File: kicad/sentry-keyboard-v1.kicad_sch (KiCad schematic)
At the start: 272 parts, among them J1 USB_C_Receptacle_USB2.0, J4 AVR-ISP-6, SW1 Reset, SW2 RotaryEncoder_Switch, U1 ATmega32U4-AU, U3 PRTR5V0U2X, Y1 16Mhz

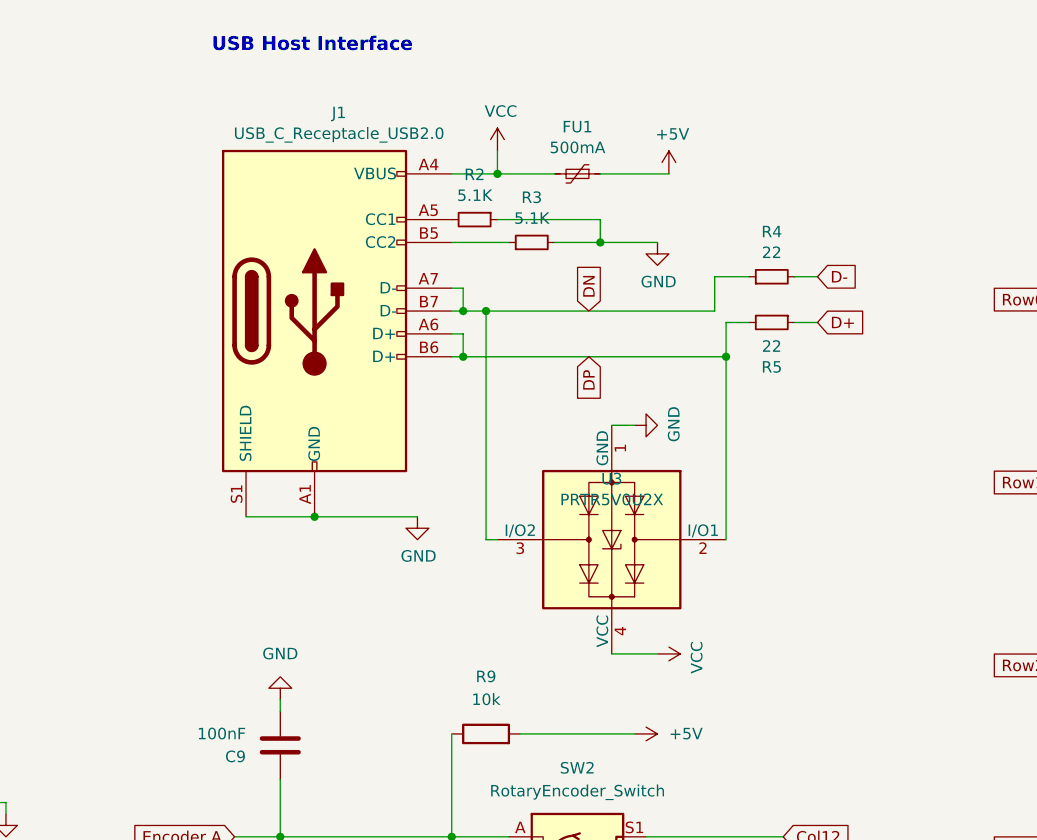
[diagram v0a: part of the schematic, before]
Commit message: Simpler USB connection
The keyboard case comes with a USBC breakout card. This card contains
the 5.1K resistors, and what looks like an ESD on them. I've removed
those from the schematics, and assigned a picoblade connector, as that
is what I think the board is currently using.
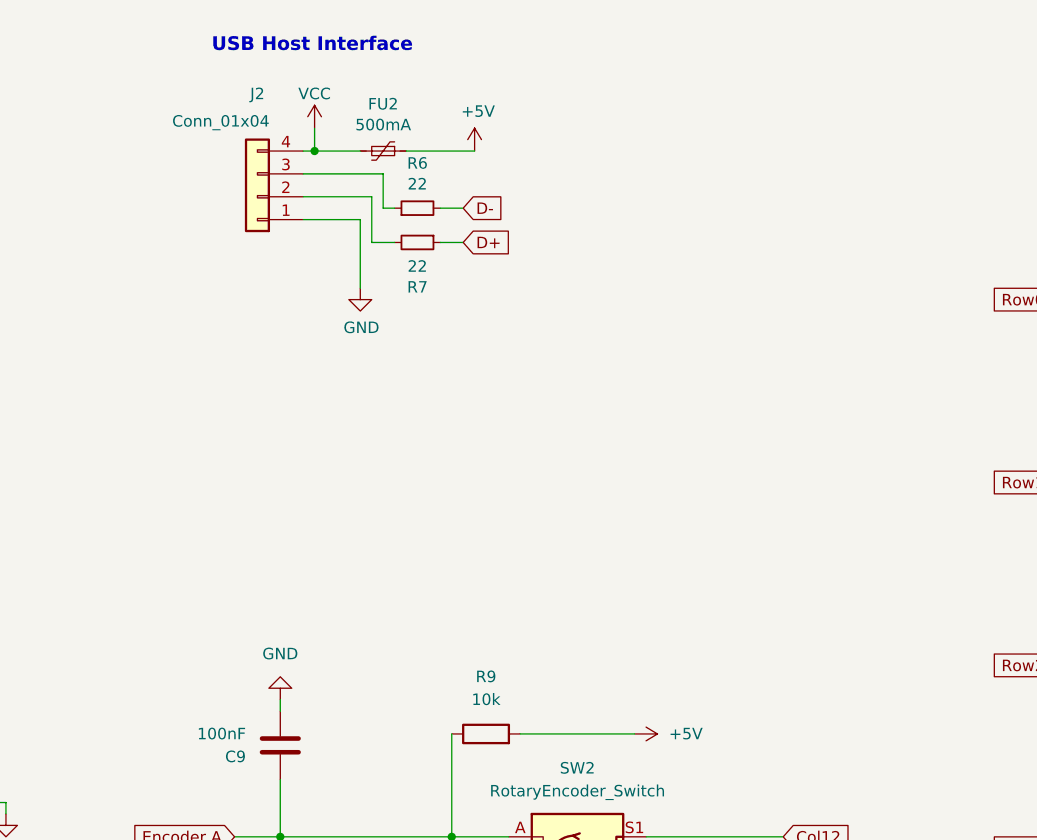
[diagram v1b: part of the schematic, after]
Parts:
- removed FU1: 500mA, Fuse:Fuse_1206_3216Metric_Pad1.42x1.75mm_HandSolder, symbol Device:Polyfuse_Small
- removed J1: USB_C_Receptacle_USB2.0, Keebio:USB_miniB_HandSolder, symbol Connector:USB_C_Receptacle_USB2.0_14P
- removed R2, R3: 5.1K, Resistor_SMD:R_0805_2012Metric, symbol Device:R_Small
- removed R4, R5: 22, Resistor_SMD:R_0805_2012Metric, symbol Device:R_Small
- removed U3: PRTR5V0U2X, Package_TO_SOT_SMD:SOT-143, symbol Power_Protection:PRTR5V0U2X
- added FU2: 500mA, Fuse:Fuse_1206_3216Metric_Pad1.42x1.75mm_HandSolder, symbol Device:Polyfuse_Small
- added J2: Conn_01x04, Connector_Molex:Molex_PicoBlade_53261-0471_1x04-1MP_P1.25mm_Horizontal, symbol Connector_Generic:Conn_01x04
- added R6, R7: 22, Resistor_SMD:R_0805_2012Metric, symbol Device:R_Small
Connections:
- net +5V: now also FU2.1
- net D+: now also R7.1
- net D-: now also R6.2
- net GND: now also J2.1 (Pin_1)
- net VCC: now also FU2.2, J2.4 (Pin_4)
- new net: J2.2 (Pin_2), R7.2
- new net: J2.3 (Pin_3), R6.1

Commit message: Update footprints and adjust positioning
I printed out the schematic and compare with the physical board and
needed to make some adjustments.
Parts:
- MXenter1: footprint Kaihl hotswap:MX-Hotswap-2.25U -> Kaihl hotswap:MX-Hotswap-2.25U-ReversedStabilizers
- MXspace1: footprint Kaihl hotswap:MX-Hotswap-6.25U -> Kaihl hotswap:MX-Hotswap-6.25U-ReversedStabilizers
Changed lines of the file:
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@@
 			)
 		)
-		(property "Footprint" "Kaihl hotswap:MX-Hotswap-6.25U"
+		(property "Footprint" "Kaihl hotswap:MX-Hotswap-6.25U-ReversedStabilizers"
 			(at 259.715 137.795 0)
 			(effects
@@
 			)
 		)
-		(property "Footprint" "Kaihl hotswap:MX-Hotswap-2.25U"
+		(property "Footprint" "Kaihl hotswap:MX-Hotswap-2.25U-ReversedStabilizers"
 			(at 352.425 97.155 0)
 			(effects

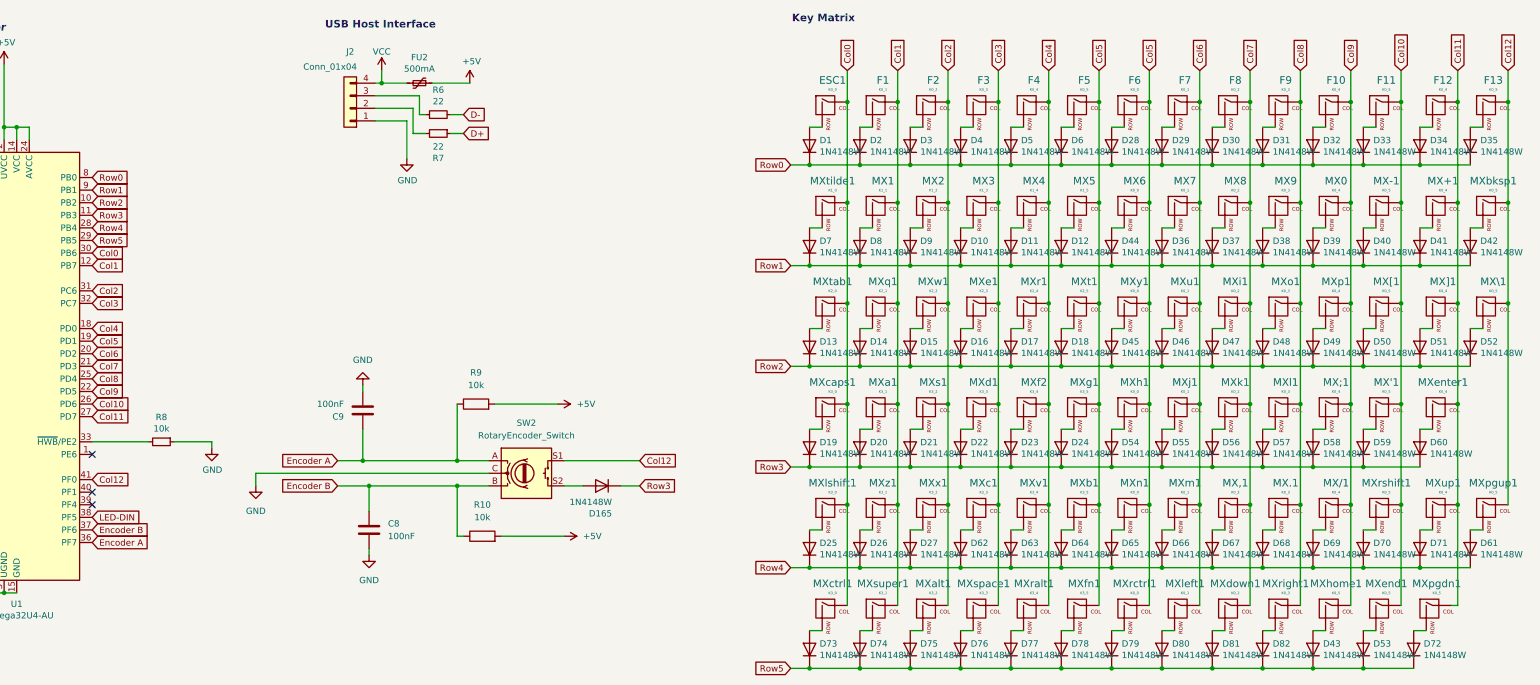
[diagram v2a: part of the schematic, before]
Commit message: Fix a big schematic mistake
I had two col5 nets! I only noticed this as I started routing the
columns. I also fixed the numbering of all the switches.
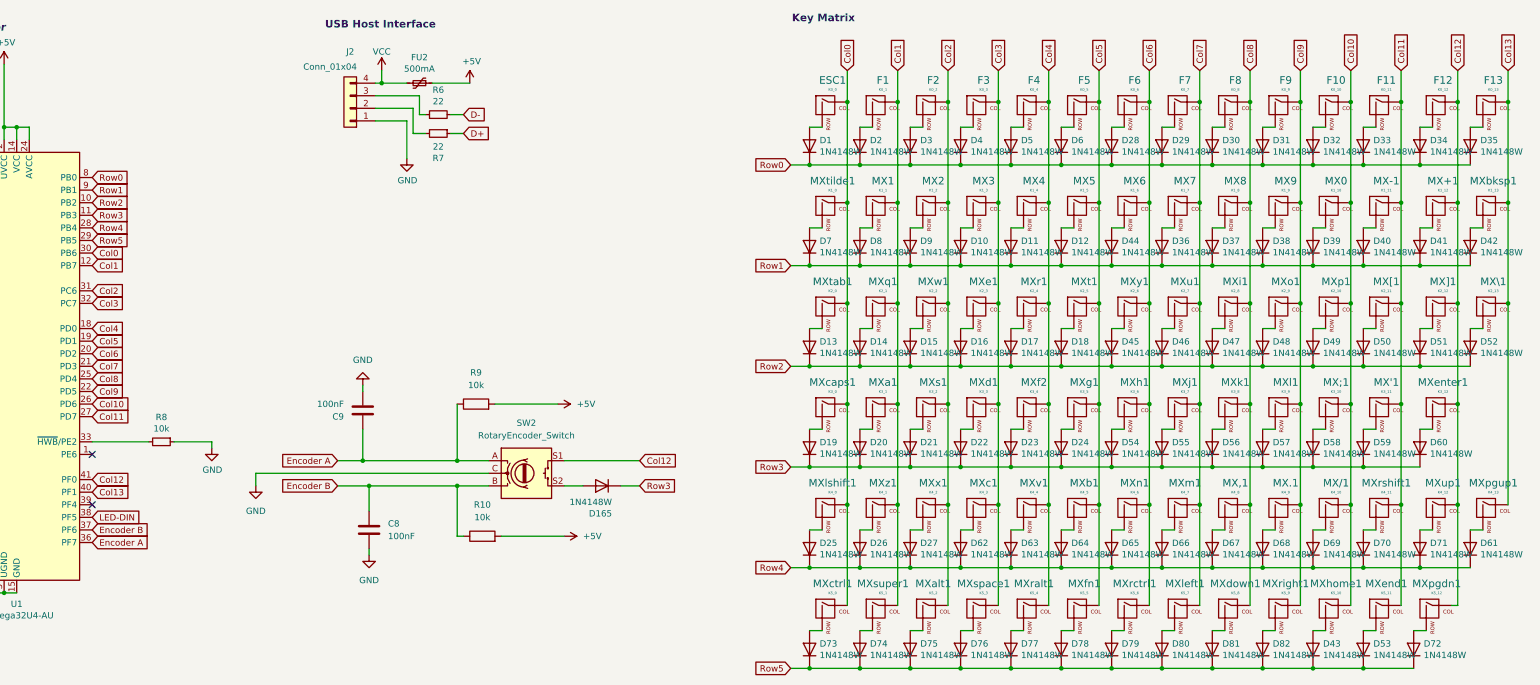
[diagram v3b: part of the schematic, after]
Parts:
- F10: value K0_4 -> K0_10
- F11: value K0_5 -> K0_11
- F12: value K0_4 -> K0_12
- F13: value K0_5 -> K0_13
- F6: value K0_0 -> K0_6
- F7: value K0_1 -> K0_7
- F8: value K0_2 -> K0_8
- F9: value K0_3 -> K0_9
- MX'1: value K0_5 -> K3_11
- MX+1: value K0_4 -> K1_12
- MX,1: value K0_2 -> K4_8
- MX-1: value K0_5 -> K1_11
- MX.1: value K0_3 -> K4_9
- MX/1: value K0_4 -> K4_10
- MX0: value K0_4 -> K1_10
- MX6: value K0_0 -> K1_6
- MX7: value K0_1 -> K1_7
- MX8: value K0_2 -> K1_8
- MX9: value K0_3 -> K1_9
- MX;1: value K0_4 -> K3_10
- MX[1: value K0_5 -> K2_11
- MX\1: value K0_5 -> K2_13
- MX]1: value K0_4 -> K2_12
- MXalt1: value K3_2 -> K5_2
- MXb1: value K3_5 -> K4_5
- MXbksp1: value K0_5 -> K1_13
- MXc1: value K3_3 -> K4_3
- MXctrl1: value K3_0 -> K5_0
- MXdown1: value K0_2 -> K5_8
- MXend1: value K0_5 -> K5_11
- MXenter1: value K0_4 -> K3_12
- MXfn1: value K3_5 -> K5_5
- MXh1: value K0_0 -> K3_6
- MXhome1: value K0_5 -> K5_10
- MXi1: value K0_2 -> K2_8
- MXj1: value K0_1 -> K3_7
- MXk1: value K0_2 -> K3_8
- MXl1: value K0_3 -> K3_9
- MXleft1: value K0_1 -> K5_7
- MXlshift1: value K3_0 -> K4_0
- MXm1: value K0_1 -> K4_7
- MXn1: value K0_0 -> K4_6
- MXo1: value K0_3 -> K2_9
- MXp1: value K0_4 -> K2_10
- MXpgdn1: value K0_5 -> K5_12
- MXpgup1: value K0_5 -> K4_13
- MXralt1: value K3_4 -> K5_4
- MXrctrl1: value K0_0 -> K5_6
- MXright1: value K0_3 -> K5_9
- MXrshift1: value K0_5 -> K4_11
- MXspace1: value K3_3 -> K5_3
- MXsuper1: value K3_1 -> K5_1
- MXu1: value K0_1 -> K2_7
- MXup1: value K0_4 -> K4_12
- MXv1: value K3_4 -> K4_4
- MXx1: value K3_2 -> K4_2
- MXy1: value K0_0 -> K2_6
- MXz1: value K3_1 -> K4_1
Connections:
- net Col10: now also F10.1 (COL), MX/1.1 (COL), MX0.1 (COL), MX;1.1 (COL), MXhome1.1 (COL), MXp1.1 (COL); no longer F11.1 (COL), MX'1.1 (COL), MX-1.1 (COL), MX[1.1 (COL), MXend1.1 (COL), MXrshift1.1 (COL)
- net Col11: now also F11.1 (COL), MX'1.1 (COL), MX-1.1 (COL), MX[1.1 (COL), MXend1.1 (COL), MXrshift1.1 (COL); no longer F12.1 (COL), MX+1.1 (COL), MX]1.1 (COL), MXenter1.1 (COL), MXpgdn1.1 (COL), MXup1.1 (COL)
- net Col12: now also F12.1 (COL), MX+1.1 (COL), MX]1.1 (COL), MXenter1.1 (COL), MXpgdn1.1 (COL), MXup1.1 (COL); no longer F13.1 (COL), MX\1.1 (COL), MXbksp1.1 (COL), MXpgup1.1 (COL)
- net Col5: no longer F6.1 (COL), MX6.1 (COL), MXh1.1 (COL), MXn1.1 (COL), MXrctrl1.1 (COL), MXy1.1 (COL)
- net Col6: now also F6.1 (COL), MX6.1 (COL), MXh1.1 (COL), MXn1.1 (COL), MXrctrl1.1 (COL), MXy1.1 (COL); no longer F7.1 (COL), MX7.1 (COL), MXj1.1 (COL), MXleft1.1 (COL), MXm1.1 (COL), MXu1.1 (COL)
- net Col7: now also F7.1 (COL), MX7.1 (COL), MXj1.1 (COL), MXleft1.1 (COL), MXm1.1 (COL), MXu1.1 (COL); no longer F8.1 (COL), MX,1.1 (COL), MX8.1 (COL), MXdown1.1 (COL), MXi1.1 (COL), MXk1.1 (COL)
- net Col8: now also F8.1 (COL), MX,1.1 (COL), MX8.1 (COL), MXdown1.1 (COL), MXi1.1 (COL), MXk1.1 (COL); no longer F9.1 (COL), MX.1.1 (COL), MX9.1 (COL), MXl1.1 (COL), MXo1.1 (COL), MXright1.1 (COL)
- net Col9: now also F9.1 (COL), MX.1.1 (COL), MX9.1 (COL), MXl1.1 (COL), MXo1.1 (COL), MXright1.1 (COL); no longer F10.1 (COL), MX/1.1 (COL), MX0.1 (COL), MX;1.1 (COL), MXhome1.1 (COL), MXp1.1 (COL)
- net Col13: now reaches U1.40 (PF1)
- net Col13: now also F13.1 (COL), MX\1.1 (COL), MXbksp1.1 (COL), MXpgup1.1 (COL)
- no-connect marks 5 -> 4

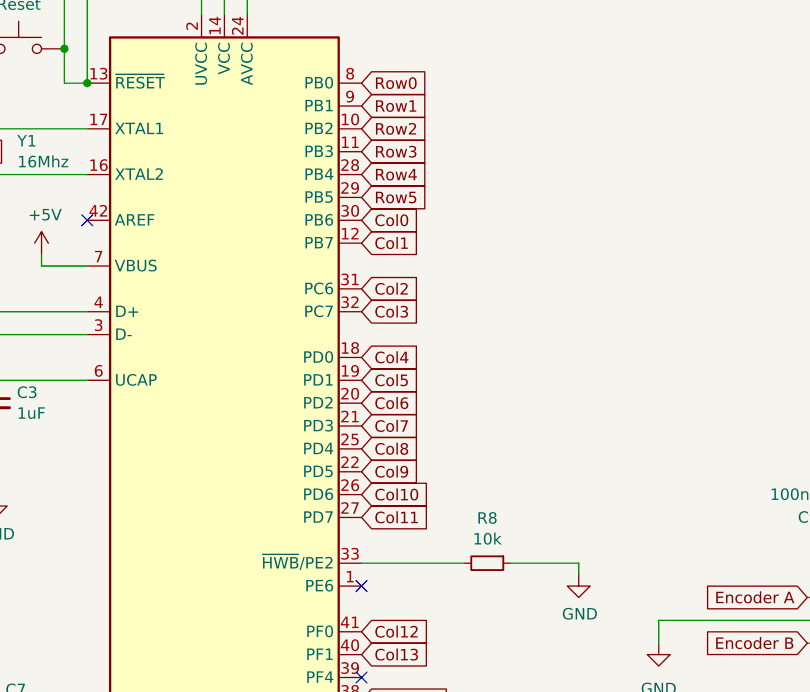
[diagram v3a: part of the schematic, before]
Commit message: Start connecting up the mcu
reassign a bunch of pins to make routing easier.
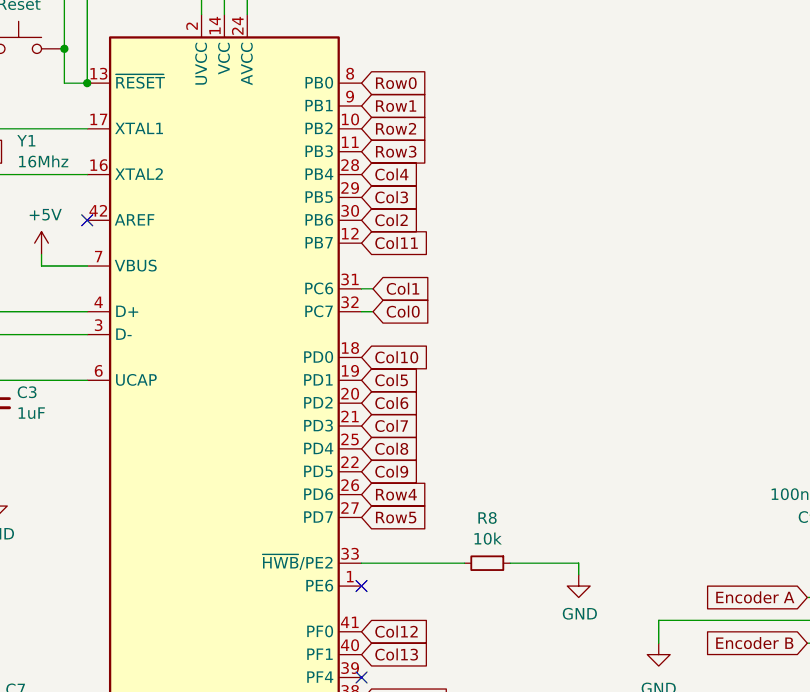
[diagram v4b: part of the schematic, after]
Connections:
- net Col0: now also U1.32 (PC7); no longer U1.30 (PB6)
- net Col1: now also U1.31 (PC6); no longer U1.12 (PB7)
- net Col10: now also U1.18 (PD0); no longer U1.26 (PD6)
- net Col11: now also U1.12 (PB7); no longer U1.27 (PD7)
- net Col2: now also U1.30 (PB6); no longer U1.31 (PC6)
- net Col3: now also U1.29 (PB5); no longer U1.32 (PC7)
- net Col4: now also U1.28 (PB4); no longer U1.18 (PD0)
- net Row4: now also U1.26 (PD6); no longer U1.28 (PB4)
- net Row5: now also U1.27 (PD7); no longer U1.29 (PB5)
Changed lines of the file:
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@@
 	(wire
 		(pts
+			(xy 96.52 72.39) (xy 97.79 72.39)
+		)
+		(stroke
+			(width 0)
+			(type default)
+		)
+	)
+	(wire
+		(pts
 			(xy 246.38 326.39) (xy 266.7 326.39)
 		)
@@
 	(wire
 		(pts
+			(xy 97.79 74.93) (xy 96.52 74.93)
+		)
+		(stroke
+			(width 0)
+			(type default)
+		)
+	)
+	(wire
+		(pts
 			(xy 350.52 74.93) (xy 350.52 95.25)
 		)
@@
 		)
 	)
-	(global_label "Col10"
-		(shape input)
-		(at 96.52 95.25 0)
-		(fields_autoplaced yes)
-		(effects
-			(font
-				(size 1.27 1.27)
-			)
-			(justify left)
-		)
-		(property "Intersheetrefs" "${INTERSHEET_REFS}"
-			(at 105.0084 95.25 0)
-			(effects
-				(font
-					(size 1.27 1.27)
-				)
-				(justify left)
-				(hide yes)
-			)
-		)
-	)
 	(global_label "Row1"
 		(shape input)
@@
 		)
 	)
-	(global_label "Row4"
+	(global_label "Col0"
 		(shape input)
-		(at 96.52 59.69 0)
-		(fields_autoplaced yes)
+		(at 97.79 74.93 0)
 		(effects
 			(font
@@
 		)
 		(property "Intersheetrefs" "${INTERSHEET_REFS}"
-			(at 104.4642 59.69 0)
+			(at 97.79 74.93 0)
 			(effects
 				(font
 					(size 1.27 1.27)
 				)
-				(justify left)
 				(hide yes)
 			)
@@
 		)
 	)
+	(global_label "Col3"
+		(shape input)
+		(at 96.52 62.23 0)
+		(fields_autoplaced yes)
+		(effects
+			(font
+				(size 1.27 1.27)
+			)
+			(justify left)
+		)
+		(property "Intersheetrefs" "${INTERSHEET_REFS}"
+			(at 103.7989 62.23 0)
+			(effects
+				(font
+					(size 1.27 1.27)
+				)
+				(justify left)
+				(hide yes)
+			)
+		)
+	)
+	(global_label "Row4"
+		(shape input)
+		(at 96.52 95.25 0)
+		(fields_autoplaced yes)
+		(effects
+			(font
+				(size 1.27 1.27)
+			)
+			(justify left)
+		)
+		(property "Intersheetrefs" "${INTERSHEET_REFS}"
+			(at 104.4642 95.25 0)
+			(effects
+				(font
+					(size 1.27 1.27)
+				)
+				(justify left)
+				(hide yes)
+			)
+		)
+	)
 	(global_label "Row0"
 		(shape input)
@@
 		)
 	)
+	(global_label "Col4"
+		(shape input)
+		(at 96.52 59.69 0)
+		(fields_autoplaced yes)
+		(effects
+			(font
+				(size 1.27 1.27)
+			)
+			(justify left)
+		)
+		(property "Intersheetrefs" "${INTERSHEET_REFS}"
+			(at 103.7989 59.69 0)
+			(effects
+				(font
+					(size 1.27 1.27)
+				)
+				(justify left)
+				(hide yes)
+			)
+		)
+	)
 	(global_label "Col3"
 		(shape input)
@@
 		)
 	)
-	(global_label "Row2"
+	(global_label "Col11"
 		(shape input)
-		(at 41.91 33.02 0)
+		(at 96.52 67.31 0)
+		(fields_autoplaced yes)
 		(effects
 			(font
@@
 		)
 		(property "Intersheetrefs" "${INTERSHEET_REFS}"
-			(at 41.91 33.02 0)
+			(at 105.0084 67.31 0)
 			(effects
 				(font
 					(size 1.27 1.27)
 				)
+				(justify left)
 				(hide yes)
 			)
 		)
 	)
-	(global_label "Row3"
+	(global_label "Row2"
 		(shape input)
-		(at 41.91 30.48 0)
+		(at 41.91 33.02 0)
 		(effects
 			(font
@@
 		)
 		(property "Intersheetrefs" "${INTERSHEET_REFS}"
-			(at 41.91 30.48 0)
+			(at 41.91 33.02 0)
 			(effects
 				(font
@@
 		)
 	)
-	(global_label "Col3"
+	(global_label "Row3"
 		(shape input)
-		(at 96.52 74.93 0)
-		(fields_autoplaced yes)
+		(at 41.91 30.48 0)
 		(effects
 			(font
@@
 		)
 		(property "Intersheetrefs" "${INTERSHEET_REFS}"
-			(at 103.7989 74.93 0)
+			(at 41.91 30.48 0)
 			(effects
 				(font
 					(size 1.27 1.27)
 				)
-				(justify left)
 				(hide yes)
 			)
@@
 		)
 	)
-	(global_label "Row5"
-		(shape input)
-		(at 96.52 62.23 0)
-		(fields_autoplaced yes)
-		(effects
-			(font
-				(size 1.27 1.27)
-			)
-			(justify left)
-		)
-		(property "Intersheetrefs" "${INTERSHEET_REFS}"
-			(at 104.4642 62.23 0)
-			(effects
-				(font
-					(size 1.27 1.27)
-				)
-				(justify left)
-				(hide yes)
-			)
-		)
-	)
-	(global_label "Col11"
-		(shape input)
-		(at 96.52 97.79 0)
-		(fields_autoplaced yes)
-		(effects
-			(font
-				(size 1.27 1.27)
-			)
-			(justify left)
-		)
-		(property "Intersheetrefs" "${INTERSHEET_REFS}"
-			(at 105.0084 97.79 0)
-			(effects
-				(font
-					(size 1.27 1.27)
-				)
-				(justify left)
-				(hide yes)
-			)
-		)
-	)
 	(global_label "Col6"
 		(shape input)
@@
 		)
 	)
-	(global_label "Col2"
+	(global_label "Col10"
 		(shape input)
-		(at 96.52 72.39 0)
+		(at 96.52 80.01 0)
+		(fields_autoplaced yes)
 		(effects
 			(font
@@
 		)
 		(property "Intersheetrefs" "${INTERSHEET_REFS}"
-			(at 96.52 72.39 0)
+			(at 105.0084 80.01 0)
 			(effects
 				(font
 					(size 1.27 1.27)
 				)
+				(justify left)
 				(hide yes)
 			)
@@
 		)
 	)
-	(global_label "Col5"
+	(global_label "Col1"
 		(shape input)
-		(at 96.52 82.55 0)
-		(fields_autoplaced yes)
+		(at 97.79 72.39 0)
 		(effects
 			(font
@@
 		)
 		(property "Intersheetrefs" "${INTERSHEET_REFS}"
-			(at 103.7989 82.55 0)
+			(at 97.79 72.39 0)
 			(effects
 				(font
 					(size 1.27 1.27)
 				)
-				(justify left)
 				(hide yes)
 			)
 		)
 	)
-	(global_label "Col4"
+	(global_label "Col5"
 		(shape input)
-		(at 96.52 80.01 0)
+		(at 96.52 82.55 0)
 		(fields_autoplaced yes)
 		(effects
@@
 		)
 		(property "Intersheetrefs" "${INTERSHEET_REFS}"
-			(at 103.7989 80.01 0)
+			(at 103.7989 82.55 0)
 			(effects
 				(font
@@
 		)
 	)
-	(global_label "Col1"
-		(shape input)
-		(at 96.52 67.31 0)
-		(effects
-			(font
-				(size 1.27 1.27)
-			)
-			(justify left)
-		)
-		(property "Intersheetrefs" "${INTERSHEET_REFS}"
-			(at 96.52 67.31 0)
-			(effects
-				(font
-					(size 1.27 1.27)
-				)
-				(hide yes)
-			)
-		)
-	)
-	(global_label "Col0"
-		(shape input)
-		(at 96.52 64.77 0)
-		(effects
-			(font
-				(size 1.27 1.27)
-			)
-			(justify left)
-		)
-		(property "Intersheetrefs" "${INTERSHEET_REFS}"
-			(at 96.52 64.77 0)
-			(effects
-				(font
-					(size 1.27 1.27)
-				)
-				(hide yes)
-			)
-		)
-	)
 	(global_label "Col11"
 		(shape input)
@@
 		)
 	)
+	(global_label "Row5"
+		(shape input)
+		(at 96.52 97.79 0)
+		(fields_autoplaced yes)
+		(effects
+			(font
+				(size 1.27 1.27)
+			)
+			(justify left)
+		)
+		(property "Intersheetrefs" "${INTERSHEET_REFS}"
+			(at 104.4642 97.79 0)
+			(effects
+				(font
+					(size 1.27 1.27)
+				)
+				(justify left)
+				(hide yes)
+			)
+		)
+	)
 	(global_label "Col9"
 		(shape input)
@@
 				(hide yes)
 			)
+		)
+	)
+	(global_label "Col2"
+		(shape input)
+		(at 96.52 64.77 0)
+		(effects
+			(font
+				(size 1.27 1.27)
+			)
+			(justify left)
+		)
+		(property "Intersheetrefs" "${INTERSHEET_REFS}"
+			(at 96.52 64.77 0)
+			(effects
+				(font
+					(size 1.27 1.27)
+				)
+				(hide yes)
+			)
